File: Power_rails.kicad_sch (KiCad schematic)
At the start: 73 parts

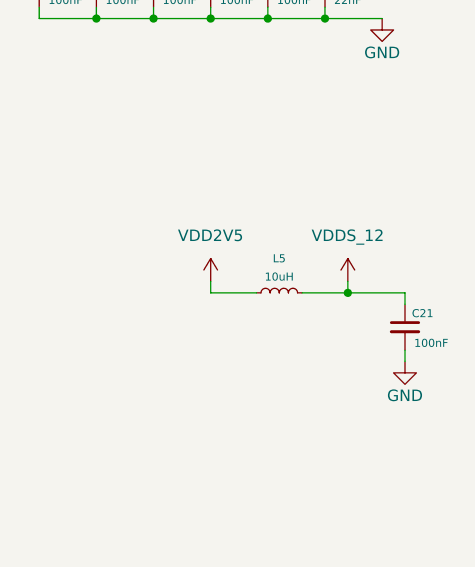
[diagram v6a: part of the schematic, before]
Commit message: finished
power planes, decoupling, ERC, DRC
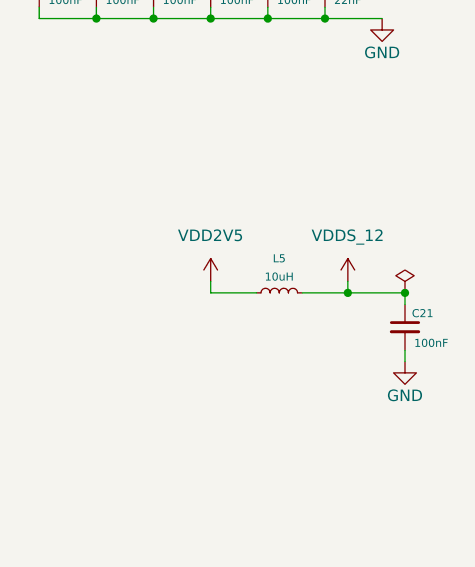
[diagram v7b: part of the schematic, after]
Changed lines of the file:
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@@
 	)
 	(junction
+		(at 251.46 101.6)
+		(diameter 0)
+		(color 0 0 0 0)
+	)
+	(junction
 		(at 68.58 158.75)
 		(diameter 0)
@@
 					(unit 1)
 				)
+			)
+		)
+	)
+	(symbol
+		(lib_id "power:PWR_FLAG")
+		(at 251.46 101.6 0)
+		(unit 1)
+		(exclude_from_sim no)
+		(in_bom yes)
+		(on_board yes)
+		(dnp no)
+		(property "Reference" "#FLG05"
+			(at 251.46 99.695 0)
+			(effects
+				(font
+					(size 1.27 1.27)
+				)
+				(hide yes)
+			)
+		)
+		(property "Value" "PWR_FLAG"
+			(at 251.206 97.79 0)
+			(effects
+				(font
+					(size 1.27 1.27)
+				)
+				(hide yes)
+			)
+		)
+		(property "Footprint" ""
+			(at 251.46 101.6 0)
+			(effects
+				(font
+					(size 1.27 1.27)
+				)
+				(hide yes)
+			)
+		)
+		(property "Datasheet" "~"
+			(at 251.46 101.6 0)
+			(effects
+				(font
+					(size 1.27 1.27)
+				)
+				(hide yes)
+			)
+		)
+		(property "Description" "Special symbol for telling ERC where power comes from"
+			(at 251.46 101.6 0)
+			(effects
+				(font
+					(size 1.27 1.27)
+				)
+				(hide yes)
+			)
+		)
+		(pin "1"
+		)
+		(instances
+			(project "PCB_Project"
+				(path "/ae14ff2f-b8e3-4dd1-9329-e73906805e39/7c344aa7-1e72-4ff4-b2c4-18ee529166e7"
+					(reference "#FLG05")
+					(unit 1)
+				)
